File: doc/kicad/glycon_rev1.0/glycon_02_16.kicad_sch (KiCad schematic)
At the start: 53 parts, among them J1 Arduino/system bus header, J2 PMOD USBUART conn, J3 Conn_01x02, J4 Conn_02x24_Odd_Even, Q1 IRF9540N, Q2 IRF9540N, SW1 SW_Push, SW2 SW_Push, U0 Z80CPU, U1 628128_DIP32_SSOP32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

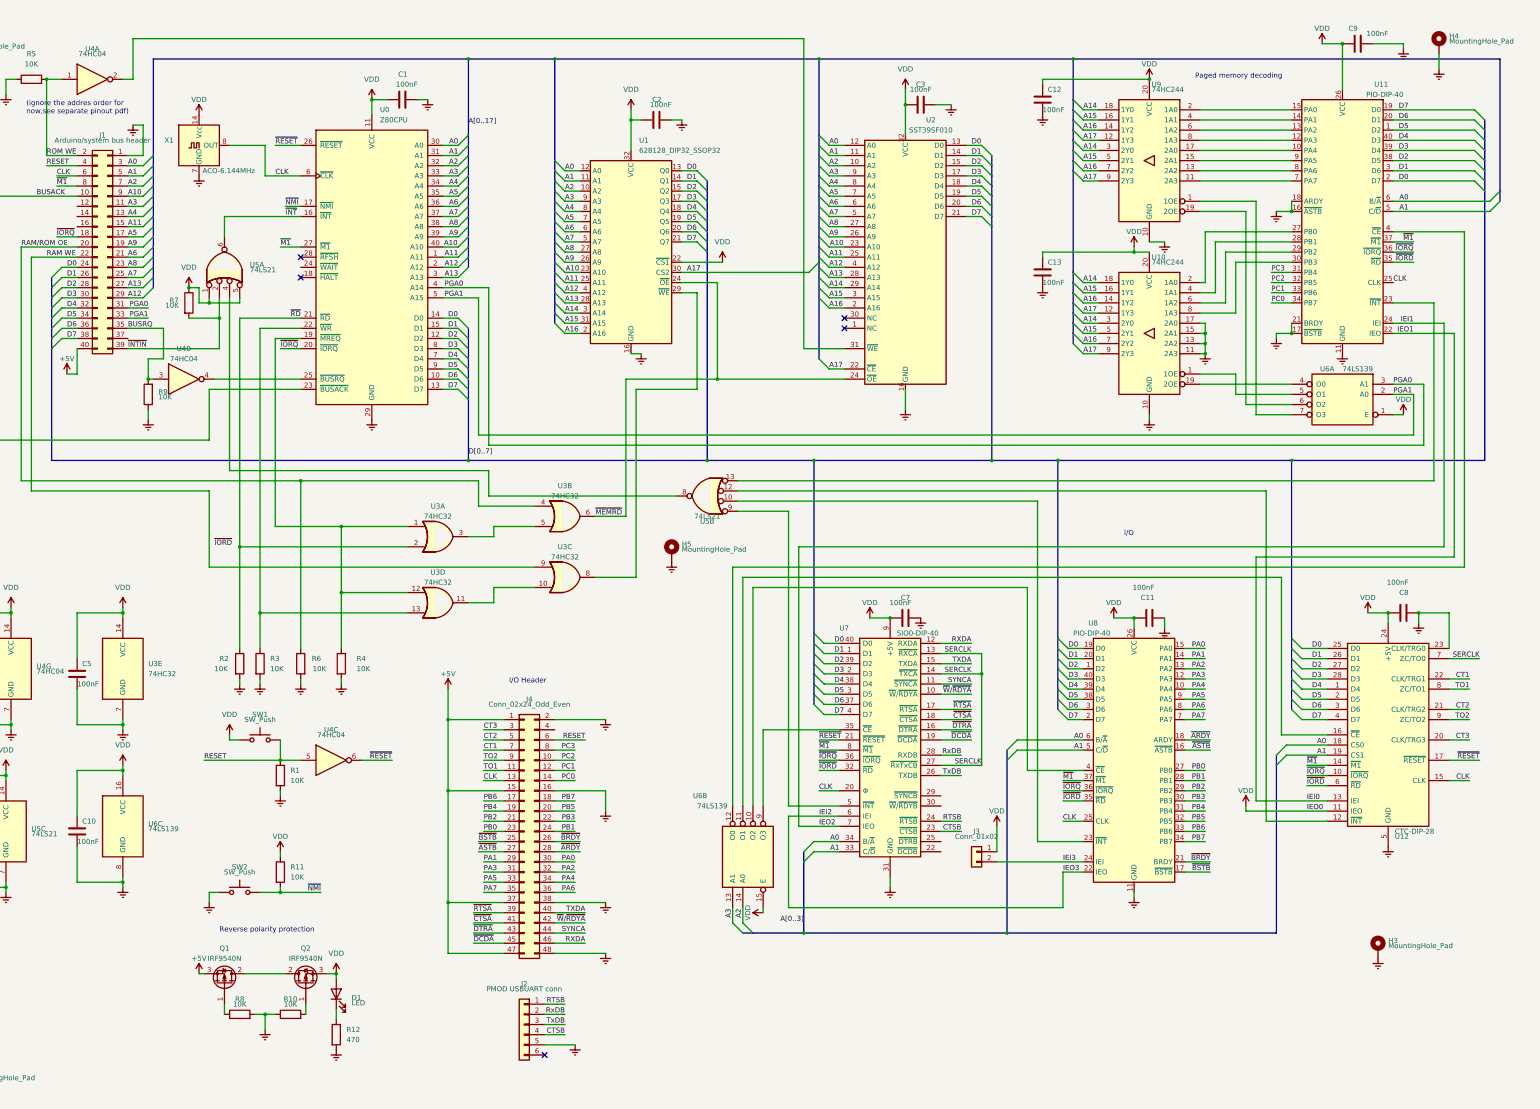
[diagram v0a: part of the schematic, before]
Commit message: update pinout schematic + add old revision of board under 'glycon_rev1.0'
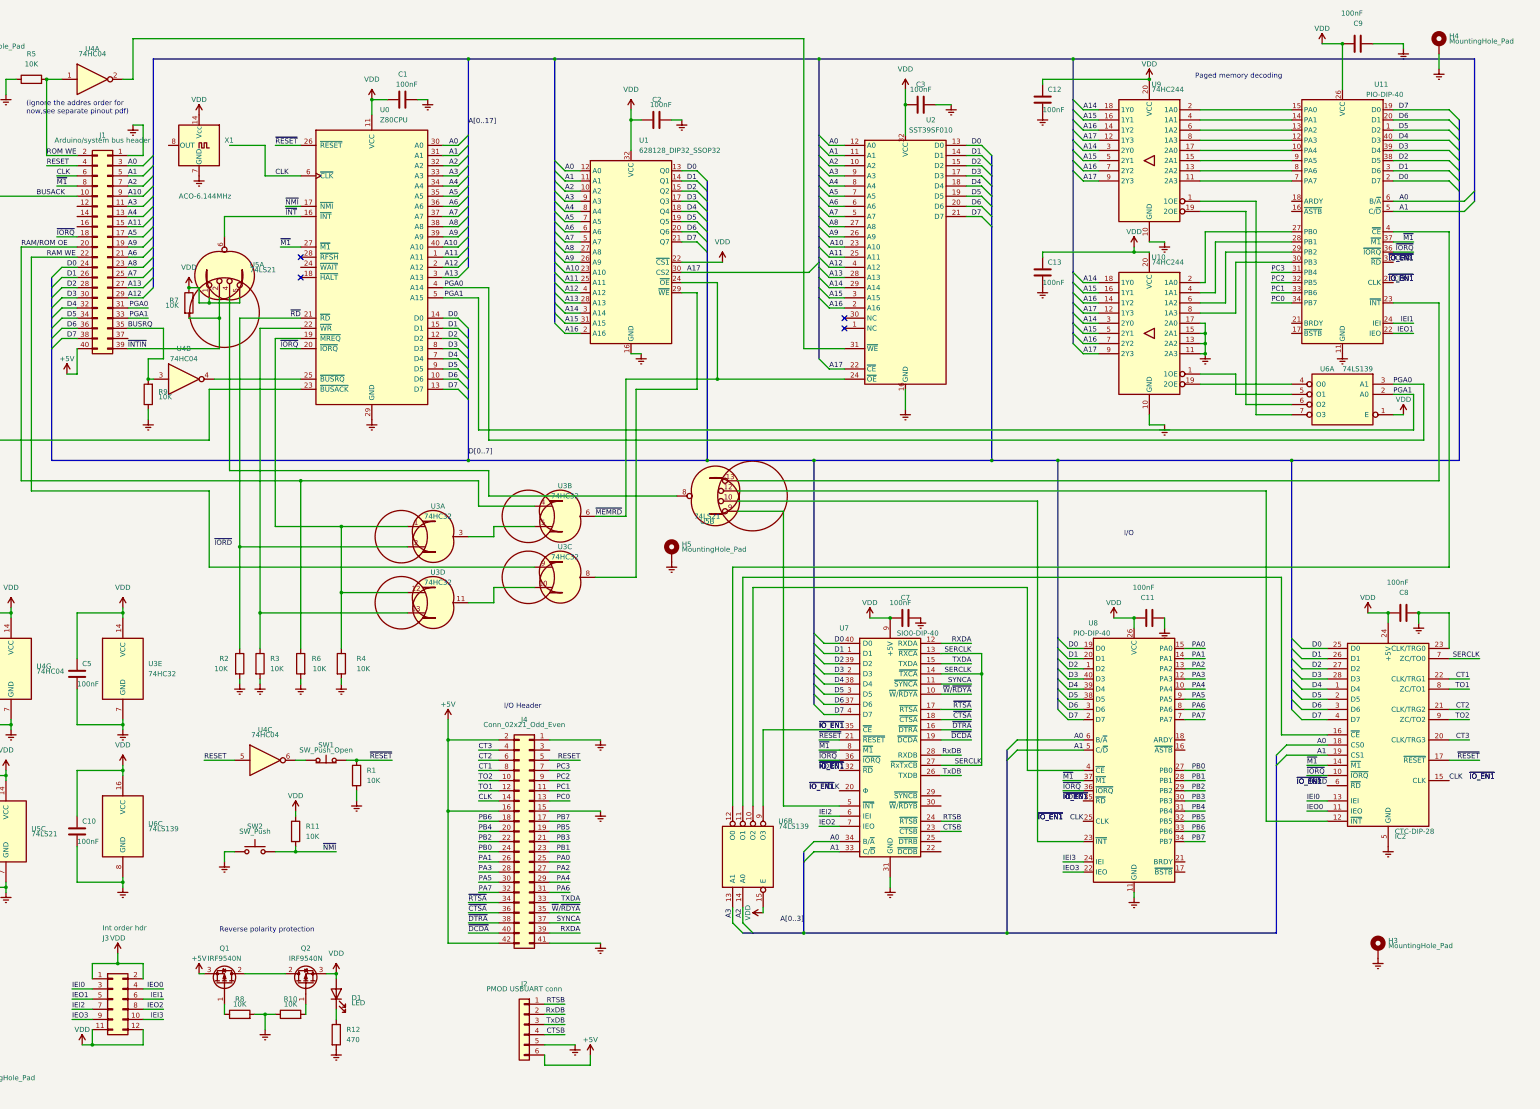
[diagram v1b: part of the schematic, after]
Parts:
- removed J3: Conn_01x02, Connector_PinHeader_2.54mm:PinHeader_1x02_P2.54mm_Vertical, symbol Connector_Generic:Conn_01x02
- removed J4: Conn_02x24_Odd_Even, Connector_PinSocket_2.54mm:PinSocket_2x24_P2.54mm_Vertical, symbol Connector_Generic:Conn_02x24_Odd_Even
- removed SW1: SW_Push, Button_Switch_THT:SW_PUSH_6mm, symbol Switch:SW_Push
- added J3: Int order hdr, Connector_PinHeader_2.54mm:PinHeader_2x06_P2.54mm_Vertical, symbol Connector_Generic:Conn_02x06_Odd_Even
- added J4: Conn_02x21_Odd_Even, Connector_PinSocket_2.54mm:PinSocket_2x21_P2.54mm_Vertical, symbol Connector_Generic:Conn_02x21_Odd_Even
- added SW1: SW_Push_Open, Button_Switch_THT:SW_PUSH_6mm, symbol Switch:SW_Push_Open
- R1, R10, R11, R12, R2, R3, R4, R5, R6, R7, R8, R9: footprint Resistor_THT:R_Axial_DIN0207_L6.3mm_D2.5mm_P10.16mm_Horizontal -> Resistor_THT:R_Axial_DIN0204_L3.6mm_D1.6mm_P5.08mm_Horizontal
- renumbered U12 to IC2
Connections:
- net +5V: now also J2.6 (Pin_6), J4.16 (Pin_16), J4.2 (Pin_2), J4.42 (Pin_42)
- net CLK: now also X1.1 (NC), J4.14 (Pin_14); no longer X1.8 (OUT)
- net CT1: now also J4.8 (Pin_8)
- net CT2: now also J4.6 (Pin_6)
- net CT3: now also J4.4 (Pin_4)
- net Earth: now also J4.1 (Pin_1), J4.15 (Pin_15), J4.41 (Pin_41); no longer U11.16 (~{ASTB}), U11.17 (~{BSTB}), U11.18 (ARDY), U11.21 (BRDY)
- net IEI0: now also J3.3 (Pin_3); no longer U11.22 (IEO)
- net IEI1: now also J3.6 (Pin_6); no longer U7.7 (IEO)
- net IEI2: now also J3.7 (Pin_7); no longer U8.22 (IEO)
- net IEI3: now also J3.10 (Pin_10)
- net PA0: now also J4.25 (Pin_25)
- net PA1: now also J4.26 (Pin_26)
- net PA2: now also J4.27 (Pin_27)
- net PA3: now also J4.28 (Pin_28)
- net PA4: now also J4.29 (Pin_29)
- net PA5: now also J4.30 (Pin_30)
- net PA6: now also J4.31 (Pin_31)
- net PA7: now also J4.32 (Pin_32)
- net PB0: now also J4.24 (Pin_24)
- net PB1: now also J4.23 (Pin_23)
- net PB2: now also J4.22 (Pin_22)
- net PB3: now also J4.21 (Pin_21)
- net PB4: now also J4.20 (Pin_20)
- net PB5: now also J4.19 (Pin_19)
- net PB6: now also J4.18 (Pin_18)
- net PB7: now also J4.17 (Pin_17)
- net PC0: now also J4.13 (Pin_13)
- net PC1: now also J4.11 (Pin_11)
- net PC2: now also J4.9 (Pin_9)
- net PC3: now also J4.7 (Pin_7)
- net RESET: now also J4.5 (Pin_5); no longer R1.1
- net RXDA: now also J4.39 (Pin_39)
- net SYNCA: now also J4.37 (Pin_37)
- net TO1: now also J4.12 (Pin_12)
- net TO2: now also J4.10 (Pin_10)
- net TXDA: now also J4.33 (Pin_33)
- net VDD: now also J3.1 (Pin_1), J3.11 (Pin_11), J3.12 (Pin_12), J3.2 (Pin_2); no longer IC2.11 (IEO)
- net ~{CTSA}: now also J4.36 (Pin_36)
- net ~{DCDA}: now also J4.40 (Pin_40)
- net ~{DTRA}: now also J4.38 (Pin_38)
- net ~{RESET}: now also R1.1, SW1.2 (B); no longer U4.6
- net ~{RTSA}: now also J4.34 (Pin_34)
- net ~{W}/~{RDYA}: now also J4.35 (Pin_35)
- net ~{IO_EN1}: now reaches U6.9 (O3), U7.35 (~{CE})
- net ~{ARDY}: no longer names the net of U8.18 (ARDY)
- net ~{ASTB}: no longer names the net of U8.16 (~{ASTB})
- net ~{BRDY}: no longer names the net of U8.21 (BRDY)
- net ~{BSTB}: no longer names the net of U8.17 (~{BSTB})
- new net: SW1.1 (A), U4.6
- new net IEO0: IC2.11 (IEO), J3.4 (Pin_4)
- new net IEO1: J3.5 (Pin_5), U11.22 (IEO)
- new net IEO2: J3.8 (Pin_8), U7.7 (IEO)
- new net IEO3: J3.9 (Pin_9), U8.22 (IEO)
- no-connect marks 5 -> 4
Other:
- moved on the sheet: R11, SW2, U3A, U3B, U3C, U3D, U4C, U5A, U5B, X1

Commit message: minor schematic updates
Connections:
- net ~{RD} is gone; now on net ~{IORD}: R2.1, U0.21 (~{RD}), U3.2
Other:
- moved on the sheet: U3A, U3B, U3C, U3D, U5A, U5B
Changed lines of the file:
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@@
+    (stroke (width 0) (type default))
+  )
+  (wire (pts (xy 81.28 143.51) (xy 87.63 143.51))
     (stroke (width 0) (type default))
   )
